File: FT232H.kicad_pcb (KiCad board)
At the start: 2 copper layers, 23 parts, among them J1 USB_B_Micro, U1 93LC56B, U2 FT232H, Y1 12MHz

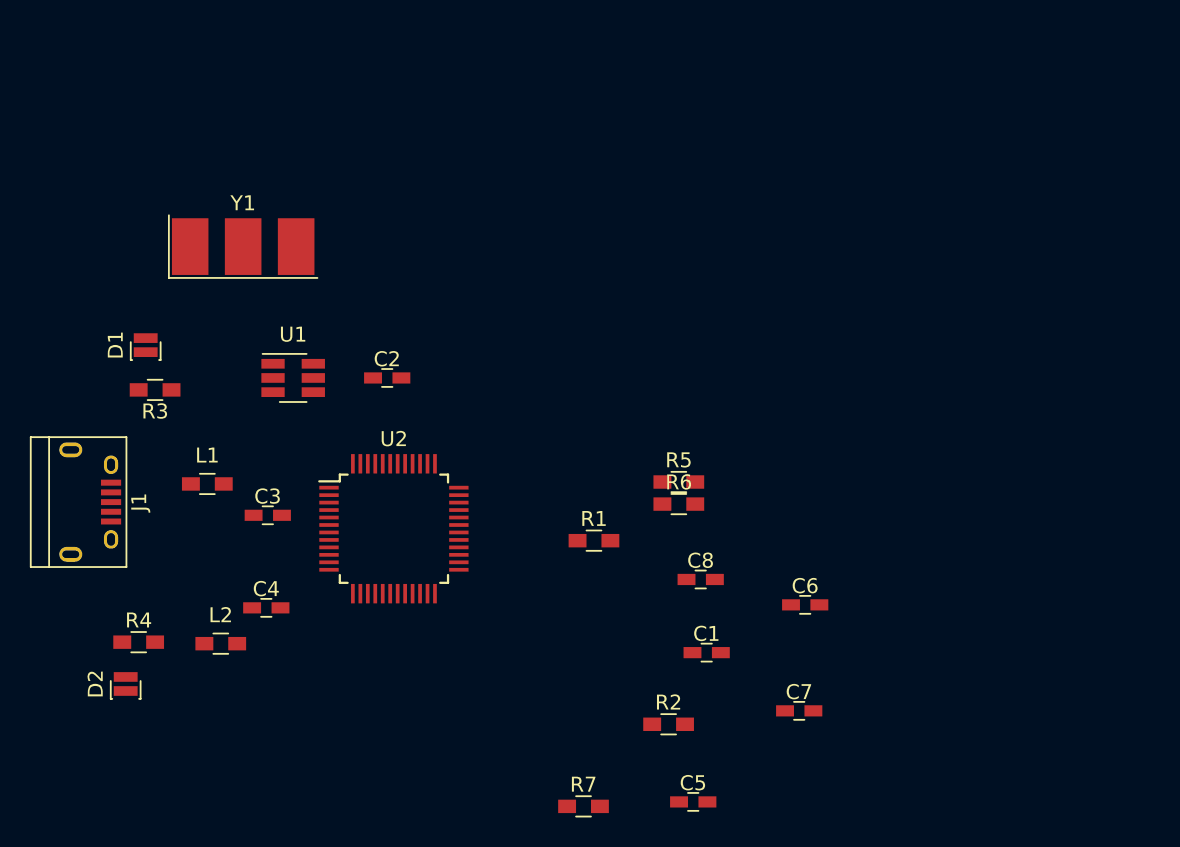
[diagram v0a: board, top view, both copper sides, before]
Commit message: Add PCB layout
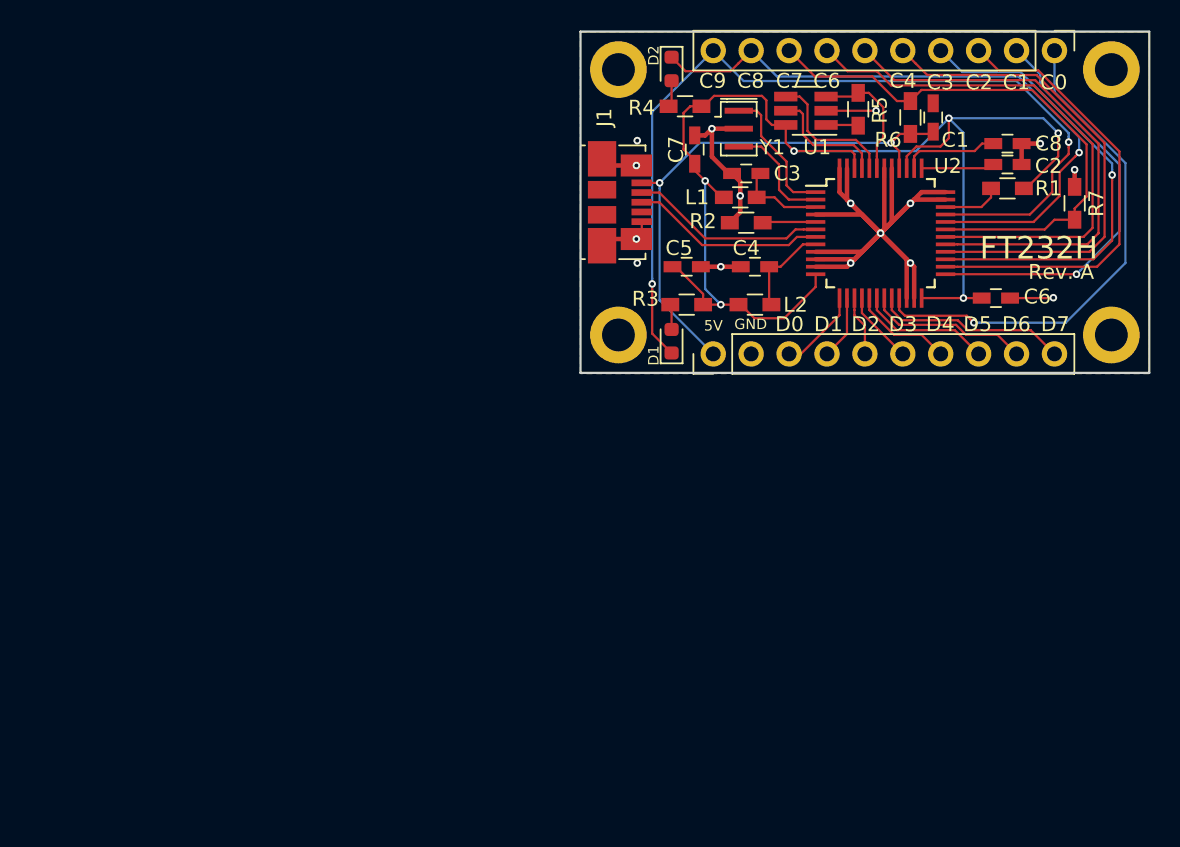
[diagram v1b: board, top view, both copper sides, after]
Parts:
- added J2: Conn_01x10, Connector_PinHeader_2.54mm:PinHeader_1x10_P2.54mm_Vertical, F.Cu at (161.3, 85.1)
- added J3: Conn_01x10, Connector_PinHeader_2.54mm:PinHeader_1x10_P2.54mm_Vertical, F.Cu at (184.2, 64.8)
- added REF**: MountingHole_2.2mm_M2_ISO14580_Pad, MountingHole:MountingHole_2.2mm_M2_ISO14580_Pad, F.Cu at (154.9, 83.8)
- added REF**: MountingHole_2.2mm_M2_ISO14580_Pad, MountingHole:MountingHole_2.2mm_M2_ISO14580_Pad, F.Cu at (160.3, 66.2)
- added REF**: MountingHole_2.2mm_M2_ISO14580_Pad, MountingHole:MountingHole_2.2mm_M2_ISO14580_Pad, F.Cu at (193.3, 83.5)
- added REF**: MountingHole_2.2mm_M2_ISO14580_Pad, MountingHole:MountingHole_2.2mm_M2_ISO14580_Pad, F.Cu at (193.2, 66.0)
- added REF**: OSHW-Logo2_9.8x8mm_SilkScreen, Symbol:OSHW-Logo2_9.8x8mm_SilkScreen, B.Cu at (166.8, 77.0)
- D1, D2: footprint LEDs:LED_0606 -> LED_SMD:LED_0603_1608Metric
- J1: footprint Connectors:USB_Micro-B -> Connector_USB:USB_Micro-B_Molex_47346-0001
- Y1: footprint Crystals:Resonator_SMD-3pin_7.2x3.0mm_HandSoldering -> Crystal:Resonator_SMD_muRata_CSTxExxV-3Pin_3.0x1.1mm
- moved D2 55.1 mm to (158.5, 66.0), turned to 270 degrees
- moved R7 52.1 mm to (185.5, 75.0), turned to 270 degrees
- moved R4 51.3 mm to (159.4, 68.5), turned to 180 degrees
- moved C2 43.9 mm to (181.0, 72.4)
- moved L2 42.4 mm to (164.1, 81.8)
- moved J1 40.7 mm to (155.0, 74.9)
- moved L1 40.5 mm to (163.1, 74.6), turned to 180 degrees
- moved C4 39.9 mm to (164.1, 79.2), turned to 180 degrees
- moved C3 39.4 mm to (163.5, 73.0), turned to 180 degrees
- moved C1 38.9 mm to (176.0, 69.2), turned to 90 degrees
- moved U1 38.7 mm to (167.5, 68.8), turned to 180 degrees
- moved C7 38.2 mm to (160.1, 71.4), turned to 90 degrees
- moved U2 38.1 mm to (172.5, 77.0)
- moved R1 36.4 mm to (181.0, 74.0)
- moved R3 36.1 mm to (159.5, 81.8)
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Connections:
- C5 pad 1: Net-(C5-Pad1) -> +3V3
- C7 pad 1: Net-(C5-Pad1) -> +3V3
- J1 pad 6: Net-(J1-Pad6) -> GND
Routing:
- net GND: track 0.00 -> 92.2 mm, vias 0 -> 16
- net +3V3: track 0.00 -> 90.5 mm, vias 0 -> 6
- net Net-(D1-Pad1): track 0.00 -> 60.8 mm, vias 0 -> 2
- net Net-(D2-Pad1): track 0.00 -> 43.5 mm, vias 0 -> 1
- net Net-(J3-Pad8): track 0.00 -> 37.6 mm
- net Net-(J3-Pad7): track 0.00 -> 36.1 mm
- net +5V: track 0.00 -> 35.8 mm, vias 0 -> 2
- net Net-(J3-Pad6): track 0.00 -> 34.8 mm
- net Net-(J3-Pad1): track 0.00 -> 34.2 mm, vias 0 -> 1
- net Net-(J3-Pad5): track 0.00 -> 33.4 mm
- net Net-(J3-Pad4): track 0.00 -> 31.4 mm, vias 0 -> 1
- net Net-(J3-Pad3): track 0.00 -> 30.7 mm
- net Net-(J3-Pad2): track 0.00 -> 27.8 mm, vias 0 -> 1
- net Net-(J1-Pad2): track 0.00 -> 13.2 mm
- net Net-(J1-Pad3): track 0.00 -> 13.1 mm
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- added copper zone on B.Cu, net GND
- added copper zone on F.Cu, net GND
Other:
- board outline added: 38.1 x 22.9 mm
- net class Default: clearance 0.2 -> 0.1524; trace_width 0.25 -> 0.1524; via_dia 0.8 -> 0.508; via_drill 0.4 -> 0.254
- net class Power added: clearance 0.1524, trace_width 0.3048, via_dia 0.508, via_drill 0.254
- rule pad_to_mask_clearance: 0.2 -> 0.0508
- rule trace_clearance: 0.2 -> 0.1524
- rule trace_min: 0.2 -> 0.1524
- rule via_min_drill: 0.3 -> 0.254
- rule via_min_size: 0.4 -> 0.508
- board text added: "5V"
- board text added: "C0"
- board text added: "C1"
- board text added: "C2"
- board text added: "C3"
- board text added: "C4"
- board text added: "C6"
- board text added: "C7"
- board text added: "C8"
- board text added: "C9"
- board text added: "D0"
- board text added: "D1"
- board text added: "D2"
- board text added: "D3"
- board text added: "D4"
- board text added: "D5"
- board text added: "D6"
- board text added: "D7"
- board text added: "FT232H"
- board text added: "GND"
- board text added: "HB9GPC"
- board text added: "Rev. A"

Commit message: Add BOM
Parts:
- R1: value 17K -> 12K
- moved R5 1.29 mm to (172.1, 69.4)
- moved R6 0.15 mm to (174.5, 69.4)
- moved U1 0.10 mm to (167.5, 68.9)
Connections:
- J1 pad 4: Net-(J1-Pad4) -> (no net)
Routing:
- net GND: track 92.2 -> 90.4 mm
- net Net-(R5-Pad2): track 2.17 -> 3.50 mm
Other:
- board text added: "C5"
